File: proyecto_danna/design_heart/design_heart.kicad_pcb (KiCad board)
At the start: 2 copper layers, 216.7 x 162 mm, 24 parts, among them Q1 BC548, U2 LM358

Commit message: update_heart
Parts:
- added D1: LED, LED_THT:LED_D5.0mm_IRGrey, F.Cu at (172.6, 105.3)
- added J1: Screw_Terminal_01x02, TerminalBlock_MetzConnect:TerminalBlock_MetzConnect_Type059_RT06302HBWC_1x02_P3.50mm_Horizontal, F.Cu at (161.1, 106.5)
- added SW1: SW_Nidec_CAS-120A1, Button_Switch_SMD:Nidec_Copal_CAS-120A, B.Cu at (186.9, 71.1)
- moved D11 166.9 mm to (189.7, 94.6)
- moved D7 146.2 mm to (179.2, 105.4)
- moved U2 145.2 mm to (165.8, 91.2), turned to -90 degrees
- moved R3 142.4 mm to (182.2, 96.2), turned to 180 degrees
- moved R4 141.4 mm to (182.2, 93.0), turned to 180 degrees
- moved D12 139.9 mm to (175.5, 66.9)
- moved R1 139.6 mm to (154.2, 114.4)
- moved RV1 136.6 mm to (178.6, 86.5), turned to 90 degrees
- moved D13 129.1 mm to (147.1, 116.2), turned to 180 degrees
- moved R7 117.2 mm to (154.1, 117.4)
- moved D10 110.4 mm to (170.6, 116.2), turned to 180 degrees
- moved D3 108.9 mm to (156.7, 126.2)
- moved R5 106.7 mm to (148.6, 84.8), turned to -90 degrees
- moved R6 103.9 mm to (145.2, 92.5), turned to 90 degrees
- moved R2 101.3 mm to (141.9, 84.9), turned to -90 degrees
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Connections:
- U2 pad 8: Net-(U1C-V+) -> +12V
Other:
- board size 216.7 x 162 mm -> 77 x 72 mm

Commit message: update_heart
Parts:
- added R8: 220, Resistor_THT:R_Axial_DIN0204_L3.6mm_D1.6mm_P7.62mm_Horizontal, F.Cu at (174.6, 97.8)
- moved R3 1.30 mm to (182.2, 94.9)
- moved R4 1.30 mm to (182.2, 91.7)
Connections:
- D1 pad 2: +12V_pre -> Net-(D1-A)
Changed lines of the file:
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@@
 	(net 19 "+12V_pre")
 	(net 20 "unconnected-(SW1-C-Pad1)")
+	(net 21 "Net-(D1-A)")
 	(footprint "Resistor_THT:R_Axial_DIN0204_L3.6mm_D1.6mm_P7.62mm_Horizontal"
 		(layer "F.Cu")
-		(at 182.16 96.17 180)
+		(at 182.21 94.87 180)
 		(descr "Resistor, Axial_DIN0204 series, Axial, Horizontal, pin pitch=7.62mm, 0.167W, length*diameter=3.6*1.6mm^2, http://cdn-reichelt.de/documents/datenblatt/B400/1_4W%23YAG.pdf")
 		(tags "Resistor Axial_DIN0204 series Axial Horizontal pin pitch 7.62mm 0.167W length 3.6mm diameter 1.6mm")
@@
 			(layers "*.Cu" "*.Mask")
 			(remove_unused_layers no)
-			(net 19 "+12V_pre")
+			(net 21 "Net-(D1-A)")
 			(pinfunction "A")
 			(pintype "passive")
@@
 	(footprint "Resistor_THT:R_Axial_DIN0204_L3.6mm_D1.6mm_P7.62mm_Horizontal"
 		(layer "F.Cu")
+		(at 174.6 97.76)
+		(descr "Resistor, Axial_DIN0204 series, Axial, Horizontal, pin pitch=7.62mm, 0.167W, length*diameter=3.6*1.6mm^2, http://cdn-reichelt.de/documents/datenblatt/B400/1_4W%23YAG.pdf")
+		(tags "Resistor Axial_DIN0204 series Axial Horizontal pin pitch 7.62mm 0.167W length 3.6mm diameter 1.6mm")
+		(property "Reference" "R8"
+			(at 3.83 -0.11 0)
+			(layer "F.SilkS")
+			(effects
+				(font
+					(size 1 1)
+					(thickness 0.15)
+				)
+			)
+		)
+		(property "Value" "220"
+			(at 3.81 1.92 0)
+			(layer "F.Fab")
+			(effects
+				(font
+					(size 1 1)
+					(thickness 0.15)
+				)
+			)
+		)
+		(property "Datasheet" "~"
+			(at 0 0 0)
+			(layer "F.Fab")
+			(hide yes)
+			(effects
+				(font
+					(size 1.27 1.27)
+					(thickness 0.15)
+				)
+			)
+		)
+		(property "Description" "Resistor, small symbol"
+			(at 0 0 0)
+			(layer "F.Fab")
+			(hide yes)
+			(effects
+				(font
+					(size 1.27 1.27)
+					(thickness 0.15)
+				)
+			)
+		)
+		(property ki_fp_filters "R_*")
+		(sheetname "/")
+		(sheetfile "design_heart.kicad_sch")
+		(attr through_hole)
+		(fp_line
+			(start 0.94 0)
+			(end 1.89 0)
+			(stroke
+				(width 0.12)
+				(type solid)
+			)
+			(layer "F.SilkS")
+		)
+		(fp_line
+			(start 6.68 0)
+			(end 5.73 0)
+			(stroke
+				(width 0.12)
+				(type solid)
+			)
+			(layer "F.SilkS")
+		)
+		(fp_rect
+			(start 1.89 -0.92)
+			(end 5.73 0.92)
+			(stroke
+				(width 0.12)
+				(type solid)
+			)
+			(fill no)
+			(layer "F.SilkS")
+		)
+		(fp_rect
+			(start -0.95 -1.05)
+			(end 8.57 1.05)
+			(stroke
+				(width 0.05)
+				(type solid)
+			)
+			(fill no)
+			(layer "F.CrtYd")
+		)
+		(fp_line
+			(start 0 0)
+			(end 2.01 0)
+			(stroke
+				(width 0.1)
+				(type solid)
+			)
+			(layer "F.Fab")
+		)
+		(fp_line
+			(start 7.62 0)
+			(end 5.61 0)
+			(stroke
+				(width 0.1)
+				(type solid)
+			)
+			(layer "F.Fab")
+		)
+		(fp_rect
+			(start 2.01 -0.8)
+			(end 5.61 0.8)
+			(stroke
+				(width 0.1)
+				(type solid)
+			)
+			(fill no)
+			(layer "F.Fab")
+		)
+		(fp_text user "${REFERENCE}"
+			(at 3.81 0 0)
+			(layer "F.Fab")
+			(effects
+				(font
+					(size 0.72 0.72)
+					(thickness 0.108)
+				)
+			)
+		)
+		(pad "1" thru_hole circle
+			(at 0 0)
+			(size 1.4 1.4)
+			(drill 0.7)
+			(layers "*.Cu" "*.Mask")
+			(remove_unused_layers no)
+			(net 19 "+12V_pre")
+			(pintype "passive")
+		)
+		(pad "2" thru_hole circle
+			(at 7.62 0)
+			(size 1.4 1.4)
+			(drill 0.7)
+			(layers "*.Cu" "*.Mask")
+			(remove_unused_layers no)
+			(net 21 "Net-(D1-A)")
+			(pintype "passive")
+		)
+		(embedded_fonts no)
+		(model "${KICAD9_3DMODEL_DIR}/Resistor_THT.3dshapes/R_Axial_DIN0204_L3.6mm_D1.6mm_P7.62mm_Horizontal.step"
+			(offset
+				(xyz 0 0 0)
+			)
+			(scale
+				(xyz 1 1 1)
+			)
+			(rotate
+				(xyz 0 0 0)
+			)
+		)
+	)
+	(footprint "Resistor_THT:R_Axial_DIN0204_L3.6mm_D1.6mm_P7.62mm_Horizontal"
+		(layer "F.Cu")
 		(at 145.22 92.47 90)
 		(descr "Resistor, Axial_DIN0204 series, Axial, Horizontal, pin pitch=7.62mm, 0.167W, length*diameter=3.6*1.6mm^2, http://cdn-reichelt.de/documents/datenblatt/B400/1_4W%23YAG.pdf")
@@
 	(footprint "Resistor_THT:R_Axial_DIN0204_L3.6mm_D1.6mm_P7.62mm_Horizontal"
 		(layer "F.Cu")
-		(at 182.19 92.98 180)
+		(at 182.24 91.68 180)
 		(descr "Resistor, Axial_DIN0204 series, Axial, Horizontal, pin pitch=7.62mm, 0.167W, length*diameter=3.6*1.6mm^2, http://cdn-reichelt.de/documents/datenblatt/B400/1_4W%23YAG.pdf")
 		(tags "Resistor Axial_DIN0204 series Axial Horizontal pin pitch 7.62mm 0.167W length 3.6mm diameter 1.6mm")

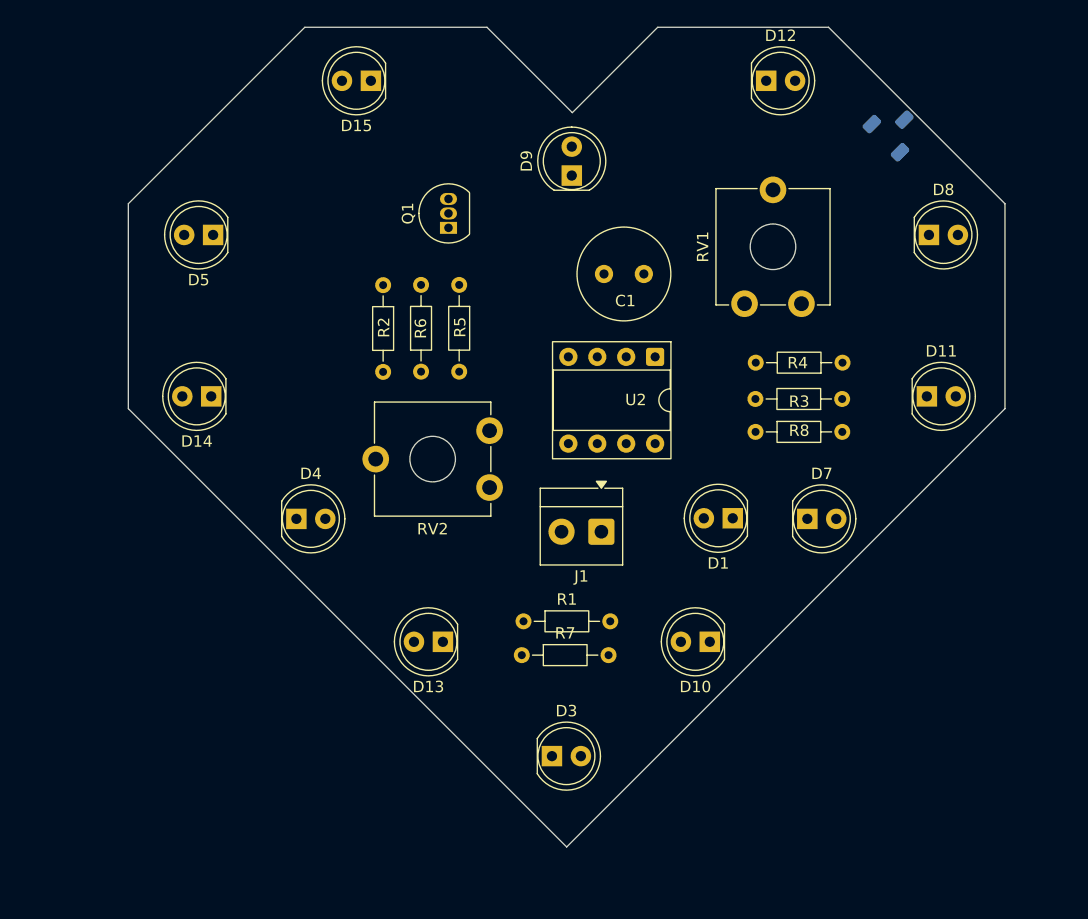
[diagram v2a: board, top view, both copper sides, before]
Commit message: update_pcb_puentes
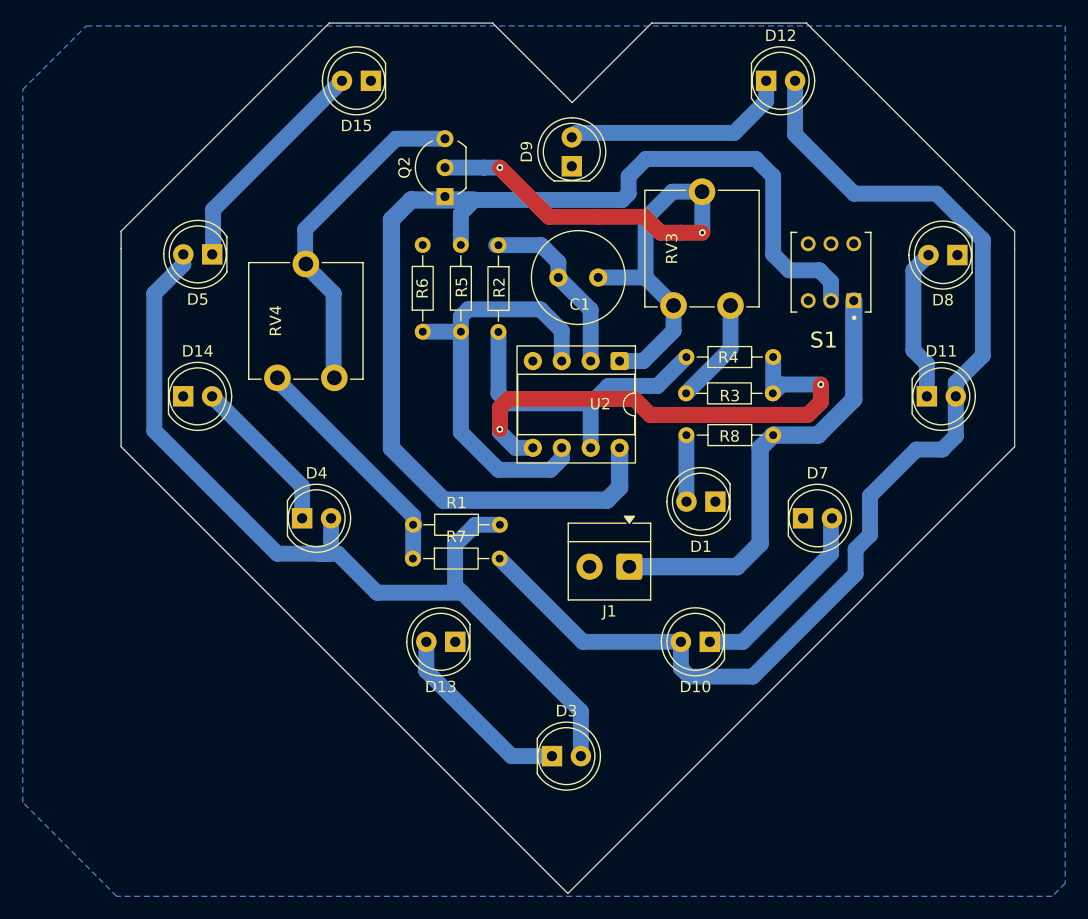
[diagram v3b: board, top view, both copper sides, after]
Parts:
- removed Q1: BC548, Package_TO_SOT_THT:TO-92_Inline
- removed RV1: 50k, Potentiometer_THT:Potentiometer_ACP_CA9-V10_Vertical_Hole
- removed RV2: 1k, Potentiometer_THT:Potentiometer_ACP_CA9-V10_Vertical_Hole
- removed SW1: SW_Nidec_CAS-120A1, Button_Switch_SMD:Nidec_Copal_CAS-120A
- added Q2: BC548, Package_TO_SOT_THT:TO-92_Inline_Wide, F.Cu at (147.3, 77.1)
- added RV3: 50k, Potentiometer_THT:Potentiometer_ACP_CA9-V10_Vertical, F.Cu at (172.4, 86.7)
- added RV4: 1k, Potentiometer_THT:Potentiometer_ACP_CA9-V10_Vertical, F.Cu at (137.6, 93.0)
- added S1: TL2230OAF140, TL2230OAF140:SW_TL2230OAF140, F.Cu at (181.2, 83.7)
- moved R1 12.9 mm to (144.5, 105.9)
- moved R7 12.8 mm to (144.5, 108.9)
- moved R2 10.7 mm to (152.0, 81.4)
- moved R3 6.11 mm to (176.1, 94.4)
- moved R4 6.11 mm to (176.1, 91.2)
- moved C1 4.02 mm to (160.8, 84.2)
- moved J1 3.93 mm to (163.5, 109.6)
- moved R6 3.51 mm to (145.4, 89.0)
- moved R5 3.51 mm to (148.7, 81.3)
- moved U2 3.14 mm to (162.7, 91.5)
- moved D8 3.06 mm to (192.3, 82.2), turned to 180 degrees
- moved D14 2.46 mm to (124.3, 94.6), turned to 0 degrees
- moved D1 2.11 mm to (171.1, 103.9)
- moved D5 1.71 mm to (126.9, 82.2)
- moved R8 1.57 mm to (176.1, 98.0), turned to 180 degrees
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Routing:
- net +12V: track 0.00 -> 102.1 mm
- net Net-(D10-A): track 0.00 -> 101.0 mm
- net Net-(D3-A): track 0.00 -> 81.3 mm
- net breath: track 0.00 -> 55.4 mm, vias 0 -> 2
- net Net-(U2B-+): track 0.00 -> 44.5 mm, vias 0 -> 2
- net +12V_pre: track 0.00 -> 39.4 mm
- net Net-(U2A-+): track 0.00 -> 37.7 mm
- net Net-(Q2-E): track 0.00 -> 29.7 mm
- net Net-(R2-Pad2): track 0.00 -> 27.8 mm
- net Net-(R1-Pad1): track 0.00 -> 20.8 mm
- net Net-(D12-K): track 0.00 -> 20.2 mm
- net Net-(D15-A): track 0.00 -> 20.0 mm
- net Net-(D10-K): track 0.00 -> 17.0 mm
- net Net-(D13-A): track 0.00 -> 16.7 mm
- net Net-(U2A--): track 0.00 -> 15.9 mm
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- added copper zone on B.Cu, net GND
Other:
- board size 77 x 72 mm -> 78.5 x 76.5 mm

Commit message: nuevo_layout
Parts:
- moved R6 30.5 mm to (174.4, 98.3), turned to 0 degrees
- moved C1 21.4 mm to (181.9, 80.6), turned to 90 degrees
- moved R5 21.4 mm to (164.5, 95.8), turned to 0 degrees
- moved D1 19.9 mm to (183.0, 88.0)
- moved R7 12.9 mm to (145.4, 96.0), turned to -90 degrees
- moved R3 12.2 mm to (164.1, 92.2), turned to 90 degrees
- moved U2 11.7 mm to (151.3, 89.0), turned to 0 degrees
- moved Q2 10.7 mm to (157.7, 79.5), turned to 180 degrees
- moved R1 10.1 mm to (142.6, 96.0), turned to -90 degrees
- moved RV3 9.96 mm to (164.9, 80.1), turned to 0 degrees
- moved R4 9.58 mm to (166.6, 92.2), turned to 90 degrees
- moved S1 8.71 mm to (173.9, 88.4), turned to 90 degrees
- moved RV4 7.57 mm to (143.8, 88.7)
- moved J1 4.73 mm to (165.9, 105.5)
- moved D9 3.34 mm to (157.1, 71.4), turned to 0 degrees
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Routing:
- net +12V: track 102.1 -> 52.5 mm
- net Net-(U2A--): track 15.9 -> 55.9 mm
- net Net-(Q2-E): track 29.7 -> 0.00 mm
- net Net-(D3-A): track 81.3 -> 63.1 mm
- net +12V_pre: track 39.4 -> 25.0 mm
- net breath: track 55.4 -> 43.5 mm, vias 2 -> 0
- net Net-(R2-Pad2): track 27.8 -> 17.7 mm
- net Net-(R1-Pad1): track 20.8 -> 11.7 mm
- net Net-(U2A-+): track 37.7 -> 44.8 mm
- net Net-(R3-Pad2): track 9.33 -> 4.86 mm
- net Net-(D10-A): track 101.0 -> 104.9 mm
- net Net-(U2B-+): track 44.5 -> 47.1 mm, vias 2 -> 0
- net Net-(D13-A): track 16.7 -> 19.3 mm
- net Net-(D1-A): track 5.84 -> 8.38 mm
- net Net-(D12-K): track 20.2 -> 17.7 mm
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
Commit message: retoques
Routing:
- net Net-(Q2-E): track 0.00 -> 11.0 mm
- net Net-(U2B-+): track 47.1 -> 48.4 mm
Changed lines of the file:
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@@
+	)
+	(segment
+		(start 151.257 89.027)
+		(end 152.781 89.027)
+		(width 1.524)
+		(layer "B.Cu")
+		(net 1)
+	)
+	(segment
+		(start 153.797 80.899)
+		(end 155.194 79.502)
+		(width 1.524)
+		(layer "B.Cu")
+		(net 1)
 	)
 	(segment
@@
 	)
 	(segment
-		(start 153.797 85.598)
-		(end 153.797 80.899)
-		(width 1.397)
+		(start 152.781 89.027)
+		(end 153.797 88.011)
+		(width 1.524)
 		(layer "B.Cu")
 		(net 1)
@@
 	)
 	(segment
-		(start 151.257 89.027)
-		(end 151.257 87.249)
-		(width 1.397)
-		(layer "B.Cu")
-		(net 1)
-	)
-	(segment
-		(start 153.797 80.899)
-		(end 155.194 79.502)
-		(width 1.397)
+		(start 153.797 88.011)
+		(end 153.797 80.899)
+		(width 1.524)
 		(layer "B.Cu")
 		(net 1)
@@
 	)
 	(segment
-		(start 152.146 86.36)
-		(end 153.035 86.36)
-		(width 1.397)
-		(layer "B.Cu")
-		(net 1)
-	)
-	(segment
 		(start 159.639 75.692)
 		(end 157.226 75.692)
@@
 		(start 155.194 77.724)
 		(end 155.194 79.502)
-		(width 1.397)
-		(layer "B.Cu")
-		(net 1)
-	)
-	(segment
-		(start 153.035 86.36)
-		(end 153.797 85.598)
-		(width 1.397)
-		(layer "B.Cu")
-		(net 1)
-	)
-	(segment
-		(start 151.257 87.249)
-		(end 152.146 86.36)
 		(width 1.397)
 		(layer "B.Cu")
@@
 		(start 138.826 88.693)
 		(end 138.826 92.217)
-		(width 1.397)
+		(width 1.524)
 		(layer "B.Cu")
 		(net 12)
@@
 		(start 138.826 92.217)
 		(end 142.621 96.012)
-		(width 1.397)
+		(width 1.524)
 		(layer "B.Cu")
 		(net 12)
@@
 		(start 142.621 96.012)
 		(end 145.415 96.012)
-		(width 1.397)
+		(width 1.524)
 		(layer "B.Cu")
 		(net 12)
@@
 	)
 	(segment
-		(start 169.164 86.36)
-		(end 169.164 81.026)
-		(width 1.016)
+		(start 157.861 82.042)
+		(end 160.655 82.042)
+		(width 1.524)
+		(layer "B.Cu")
+		(net 16)
+	)
+	(segment
+		(start 160.655 82.042)
+		(end 161.036 81.661)
+		(width 1.524)
+		(layer "B.Cu")
+		(net 16)
+	)
+	(segment
+		(start 162.5355 78.2565)
+		(end 167.2835 78.2565)
+		(width 1.143)
+		(layer "B.Cu")
+		(net 16)
+	)
+	(segment
+		(start 155.575 84.328)
+		(end 157.861 82.042)
+		(width 1.524)
 		(layer "B.Cu")
 		(net 16)
@@
 	(segment
 		(start 157.099 96.647)
-		(end 158.877 96.647)
-		(width 1.016)
-		(layer "B.Cu")
-		(net 16)
-	)
-	(segment
-		(start 164.147692 78.193)
-		(end 163.047 79.293692)
-		(width 1.016)
-		(layer "B.Cu")
-		(net 16)
-	)
-	(segment
-		(start 165.704308 78.193)
-		(end 164.147692 78.193)
-		(width 1.016)
-		(layer "B.Cu")
-		(net 16)
-	)
-	(segment
-		(start 162.743494 80.264)
-		(end 160.782 80.264)
-		(width 1.016)
-		(layer "B.Cu")
-		(net 16)
-	)
-	(segment
-		(start 166.805 80.264)
-		(end 166.805 79.293692)
-		(width 1.016)
-		(layer "B.Cu")
-		(net 16)
-	)
-	(segment
-		(start 155.575 95.123)
+		(end 155.575 95.123)
+		(width 1.524)
+		(layer "B.Cu")
+		(net 16)
+	)
+	(segment
+		(start 167.2835 78.2565)
+		(end 169.164 80.137)
+		(width 1.143)
+		(layer "B.Cu")
+		(net 16)
+	)
+	(segment
+		(start 158.877 96.647)
 		(end 157.099 96.647)
-		(width 1.016)
-		(layer "B.Cu")
-		(net 16)
-	)
-	(segment
-		(start 169.164 81.026)
-		(end 168.402 80.264)
-		(width 1.016)
-		(layer "B.Cu")
-		(net 16)
-	)
-	(segment
-		(start 163.047 79.960494)
-		(end 162.743494 80.264)
-		(width 1.016)
+		(width 1.524)
 		(layer "B.Cu")
 		(net 16)
@@
 		(start 166.624 92.202)
 		(end 164.084 92.202)
-		(width 1.016)
-		(layer "B.Cu")
-		(net 16)
-	)
-	(segment
-		(start 168.402 80.264)
-		(end 166.805 80.264)
-		(width 1.016)
-		(layer "B.Cu")
-		(net 16)
-	)
-	(segment
-		(start 166.805 79.293692)
-		(end 165.704308 78.193)
-		(width 1.016)
-		(layer "B.Cu")
-		(net 16)
-	)
-	(segment
-		(start 160.782 80.264)
-		(end 155.575 85.471)
-		(width 1.016)
+		(width 1.397)
+		(layer "B.Cu")
+		(net 16)
+	)
+	(segment
+		(start 169.164 80.137)
+		(end 169.164 86.36)
+		(width 1.524)
+		(layer "B.Cu")
+		(net 16)
+	)
+	(segment
+		(start 155.575 95.123)
+		(end 155.575 84.328)
+		(width 1.524)
+		(layer "B.Cu")
+		(net 16)
+	)
+	(segment
+		(start 166.624 88.9)
+		(end 169.164 86.36)
+		(width 1.397)
 		(layer "B.Cu")
 		(net 16)
@@
 		(start 166.624 92.202)
 		(end 166.624 88.9)
-		(width 1.016)
-		(layer "B.Cu")
-		(net 16)
-	)
-	(segment
-		(start 166.624 88.9)
-		(end 169.164 86.36)
-		(width 1.016)
-		(layer "B.Cu")
-		(net 16)
-	)
-	(segment
-		(start 163.047 79.293692)
-		(end 163.047 79.960494)
-		(width 1.016)
-		(layer "B.Cu")
-		(net 16)
-	)
-	(segment
-		(start 155.575 85.471)
-		(end 155.575 95.123)
-		(width 1.016)
+		(width 1.397)
+		(layer "B.Cu")
+		(net 16)
+	)
+	(segment
+		(start 161.036 79.756)
+		(end 162.5355 78.2565)
+		(width 1.143)
+		(layer "B.Cu")
+		(net 16)
+	)
+	(segment
+		(start 161.036 81.661)
+		(end 161.036 79.756)
+		(width 1.524)
 		(layer "B.Cu")
 		(net 16)
@@
 		(net 19)
 	)
+	(segment
+		(start 143.826 88.693)
+		(end 143.826 81.193)
+		(width 1.524)
+		(layer "B.Cu")
+		(net 24)
+	)
+	(segment
+		(start 143.826 81.193)
+		(end 141.326 78.693)
+		(width 1.524)
+		(layer "B.Cu")
+		(net 24)
+	)
 	(zone

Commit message: retoques
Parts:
- moved D9 1.28 mm to (157.2, 70.1)
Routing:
- net GND: track 0.00 -> 19.1 mm, vias 0 -> 2
- net Net-(Q2-E): track 11.0 -> 28.8 mm, vias 0 -> 2
- net Net-(D13-A): track 19.3 -> 17.5 mm
- net Net-(D11-K): track 12.5 -> 13.6 mm
- net +12V_pre: track 25.0 -> 26.1 mm
- net Net-(D12-K): track 17.7 -> 17.1 mm
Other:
- outline, holes or cut-outs redrawn

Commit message: avance
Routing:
- net Net-(R2-Pad2): track 17.7 -> 19.5 mm
- net +12V_pre: track 26.1 -> 26.7 mm
